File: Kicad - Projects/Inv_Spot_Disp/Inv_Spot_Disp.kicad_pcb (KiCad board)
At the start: 2 copper layers, 128.6 x 75.3 mm, 39 parts, among them J1 PWM_Out, J2 Power_Supply, J3 Trigger, J4 Prog, SW1 1, SW2 2, SW3 3, SW4 4, SW5 SW_Push, U1 STM32F030F4Px, U2 NHD-0420H1Z, U3 AMS1117-3.3, U4 LKS561, U5 L7805, U6 LTV-817S

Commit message: Cotações
Cotações
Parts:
- removed C12: 104, Capacitor_SMD:C_1206_3216Metric_Pad1.33x1.80mm_HandSolder
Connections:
- U1 pad 6: Current_Sense -> unconnected-(U1-PA0-Pad6)
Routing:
- net GND: track 346.7 -> 336.0 mm, vias 17 -> 16
- net Current_Sense: track 7.07 -> 0.00 mm
- net 5V: track 76.5 -> 78.0 mm, vias 2 -> 1
- net Net-(U2-VO): track 9.90 -> 8.50 mm
- net Enable: track 41.7 -> 40.5 mm
- net D7: track 22.9 -> 22.3 mm
- net RS: track 49.0 -> 48.5 mm
- net 3V3: vias 1 -> 0

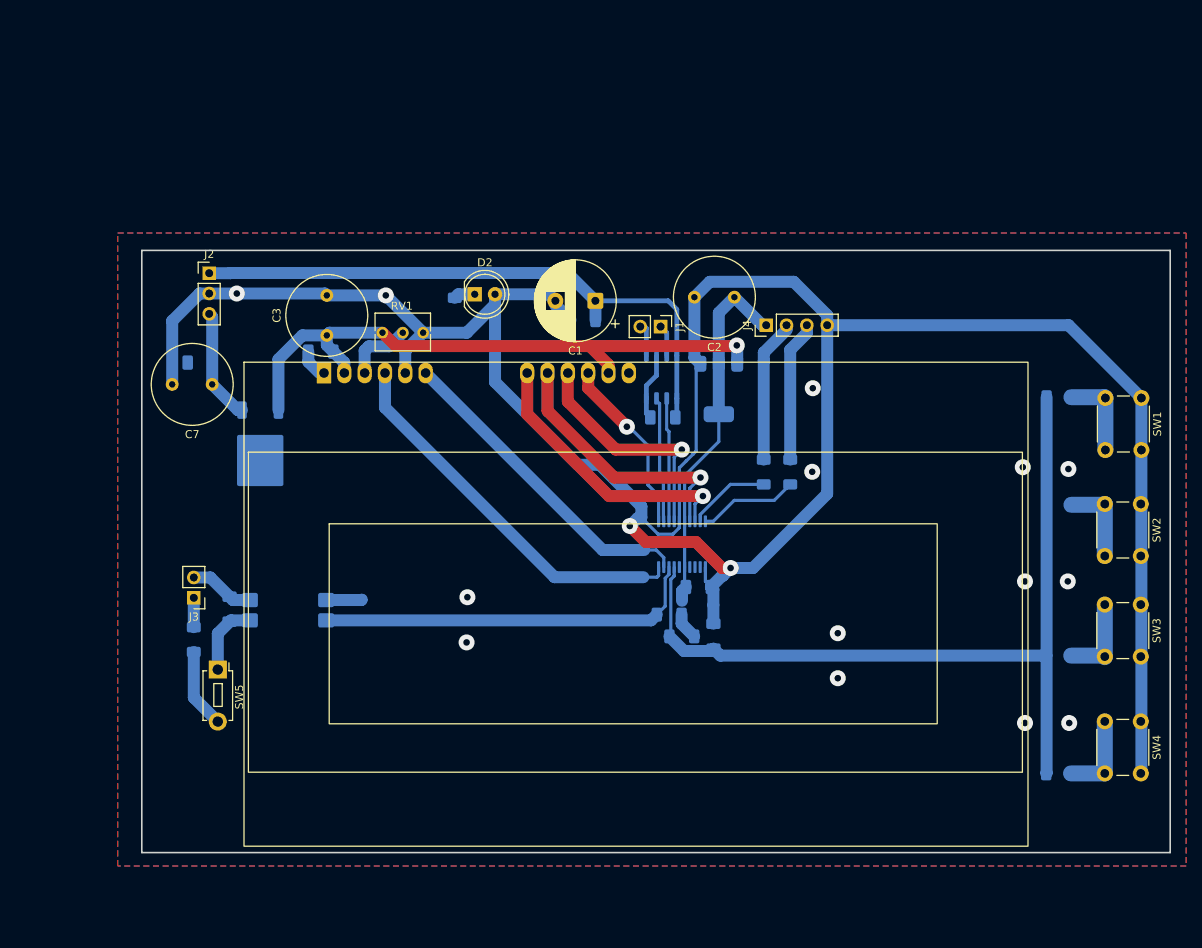
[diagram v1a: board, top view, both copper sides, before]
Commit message: Adicionada Fuaração
Adicionada furação de montagem na placa de display, 4 furos M3 nos cantos da placa
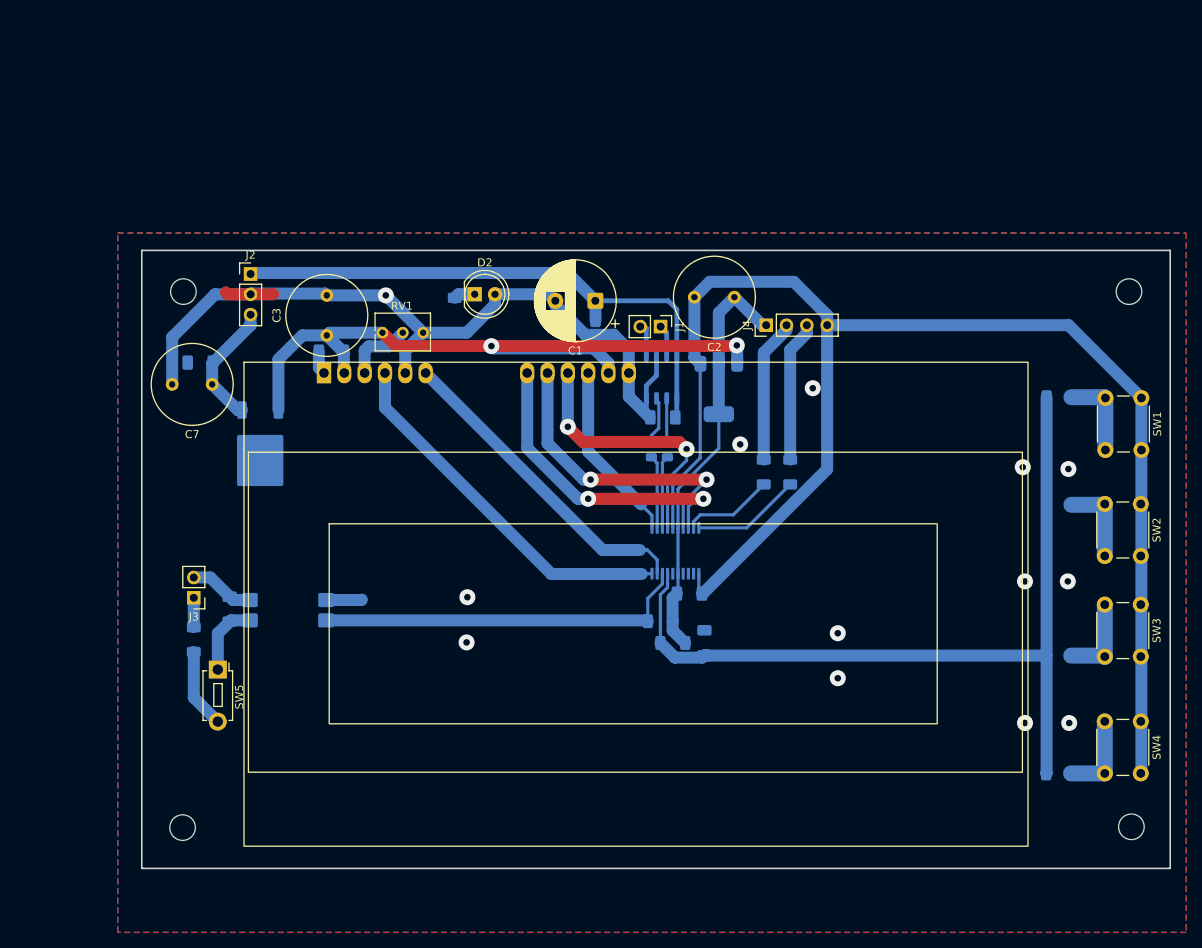
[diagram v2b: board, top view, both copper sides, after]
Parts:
- added R13: 470, Resistor_SMD:R_0805_2012Metric, B.Cu at (94.2, 74.3)
- added R15: 470, Resistor_SMD:R_0805_2012Metric, B.Cu at (92.2, 74.3)
- added REF**: MountingHole_3.2mm_M3, MountingHole:MountingHole_3.2mm_M3, F.Cu at (33.6, 121.5)
- added REF**: MountingHole_3.2mm_M3, MountingHole:MountingHole_3.2mm_M3, F.Cu at (33.7, 54.5)
- added REF**: MountingHole_3.2mm_M3, MountingHole:MountingHole_3.2mm_M3, F.Cu at (151.9, 54.5)
- added REF**: MountingHole_3.2mm_M3, MountingHole:MountingHole_3.2mm_M3, F.Cu at (152.2, 121.4)
- moved J2 5.18 mm to (42.1, 52.3)
- moved C4 1.40 mm to (97.0, 92.2)
- moved C6 1.40 mm to (98.8, 98.4)
- moved R1 1.40 mm to (94.9, 98.4)
- moved R9 1.40 mm to (93.3, 95.7)
- moved C5 1.33 mm to (52.2, 62.0)
- moved U1 1.17 mm to (95.2, 86.9)
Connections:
- U4 pad 2: PWM_H -> Net-(U4-Hin)
- U4 pad 3: PWM_L -> Net-(U4-Lin)
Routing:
- net GND: track 336.0 -> 294.3 mm, vias 16 -> 13
- net 5V: track 78.0 -> 90.5 mm, vias 1 -> 2
- net D7: track 22.3 -> 32.0 mm, vias 1 -> 0
- net PWM_L: track 15.7 -> 9.13 mm
- net PWM_H: track 15.5 -> 9.08 mm
- net Net-(U4-Lin): track 0.00 -> 6.04 mm
- net Net-(U4-Hin): track 0.00 -> 5.45 mm
- net 15V: track 76.3 -> 71.2 mm
- net D5: track 33.3 -> 37.8 mm, vias 1 -> 2
- net D4: track 34.9 -> 39.0 mm, vias 1 -> 2
- net D6: track 29.7 -> 33.6 mm, vias 1 -> 2
- net 3V3: track 49.6 -> 52.5 mm
- net RS: track 48.5 -> 46.3 mm
- net 7V: track 14.0 -> 15.8 mm
- net Trigger: track 48.2 -> 46.9 mm
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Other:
- board size 128.6 x 75.3 mm -> 128.6 x 77.2 mm

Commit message: Finalização da Nova Placa de Potência
Dissipadores reorientados e reposicionados para melhor fluxo de ar

Ajuste dos footprints para dissipadores

Adição de resistores na placa de display para melhor proteção do STM32 e redução do brilho da LCD
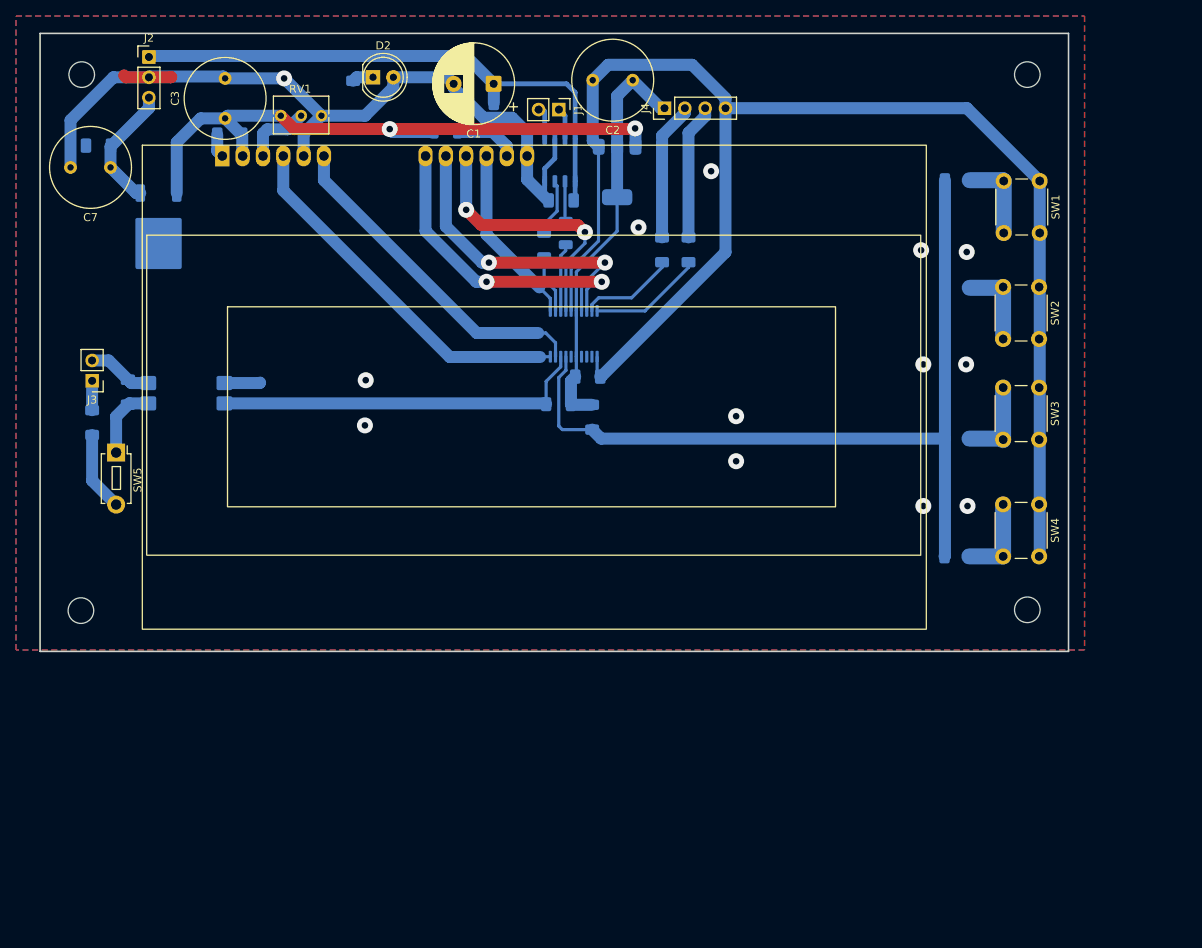
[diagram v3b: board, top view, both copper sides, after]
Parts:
- removed C6: 104, Capacitor_SMD:C_1206_3216Metric_Pad1.33x1.80mm_HandSolder
- added R16: 100, Resistor_SMD:R_1206_3216Metric, B.Cu at (66.5, 34.5)
- R1: value 2k -> 2k2
- R13, R15: value 470 -> 100; footprint Resistor_SMD:R_0805_2012Metric -> Resistor_SMD:R_1206_3216Metric
- R2: value 1k -> 10k
- R3: value 2k -> 4k7
- R4: value 4k -> 2k2
- R5: value 10k -> 1k
- R8: value 1k8 -> 2k2
- R9: value 3k3 -> 4k7
- moved R11 30.5 mm to (93.5, 49.3)
- moved R12 30.5 mm to (96.8, 49.3)
- moved REF** 30.1 mm to (139.2, 94.3)
- moved R1 30.0 mm to (84.8, 70.2), turned to -90 degrees
- moved R3 30.0 mm to (130.4, 54.0)
- moved U1 30.0 mm to (82.5, 59.8)
- moved C2 30.0 mm to (89.9, 28.1)
- moved J4 30.0 mm to (93.8, 31.6)
- moved C1 30.0 mm to (72.5, 28.5)
- moved C3 30.0 mm to (38.9, 32.9)
- moved C4 30.0 mm to (84.2, 65.1)
- moved C5 30.0 mm to (39.5, 34.9)
- moved C8 30.0 mm to (23.1, 36.2)
- moved C9 30.0 mm to (26.8, 67.1)
- moved D2 30.0 mm to (57.4, 27.7)
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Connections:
- U2 pad 15: 5V -> Net-(U2-A)
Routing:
- net 5V: track 90.5 -> 79.3 mm
- net Net-(U2-A): track 0.00 -> 7.75 mm
- net Enable: track 40.4 -> 42.1 mm
- net PWM_L: track 9.13 -> 7.43 mm
- net Net-(U4-Lin): track 6.04 -> 7.34 mm
- net 3V3: track 52.5 -> 51.8 mm
- net SWWDIO: track 11.5 -> 12.1 mm
- net SWCLK: track 13.7 -> 14.3 mm
- net Net-(J4-Pin_3): track 17.7 -> 17.0 mm
- net Net-(J4-Pin_2): track 18.0 -> 17.3 mm
- net PWM_H: track 9.08 -> 8.53 mm

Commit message: Preparação para Manufatura
Validação de footprints

Serigrafia movida para melhorar legibilidade

Backup de versão com trafo anterior salvo

Adição de snippet de código para ativação da proteção térmica
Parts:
- removed the REF** at (20.9, 94.4)
- removed the REF** at (21.0, 27.4)
- removed the REF** at (139.2, 27.4)
- removed the REF** at (139.2, 94.3)
- added R10: 4k7, Resistor_SMD:R_1206_3216Metric_Pad1.30x1.75mm_HandSolder, B.Cu at (88.5, 68.9)
- added R17: 2k2, Resistor_SMD:R_1206_3216Metric_Pad1.30x1.75mm_HandSolder, B.Cu at (106.2, 61.8)
- added REF**: Hexagonal-M3, Board_Fixation:Hexagonal-M3, B.Cu at (139.2, 20.5)
- added REF**: Hexagonal-M3, Board_Fixation:Hexagonal-M3, B.Cu at (20.9, 87.5)
- added REF**: Hexagonal-M3, Board_Fixation:Hexagonal-M3, B.Cu at (21.0, 20.6)
- added REF**: Hexagonal-M3, Board_Fixation:Hexagonal-M3, B.Cu at (139.2, 87.5)
- added U7: LTV-817S, Package_DIP:SMDIP-4_W9.53mm, B.Cu at (101.2, 67.9)
- moved C5 5.73 mm to (39.8, 40.6)
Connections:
- U1 pad 3: unconnected-(U1-PF1-Pad3) -> Temp_Sig
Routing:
- net 15V: track 71.2 -> 137.3 mm
- net GND: track 294.3 -> 231.1 mm, vias 13 -> 10
- net Temp_Sig: track 0.00 -> 18.2 mm
- net Net-(C11-Pad1): track 0.00 -> 3.38 mm
- net 5V: track 79.3 -> 82.3 mm
- net 3V3: track 51.8 -> 54.1 mm
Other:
- board text added: "Hexagonal-M3"
- board text added: "SPOTCAR INVERSORA PLACA DE DISPLAY REV 07/10/26 - V1.0.0"

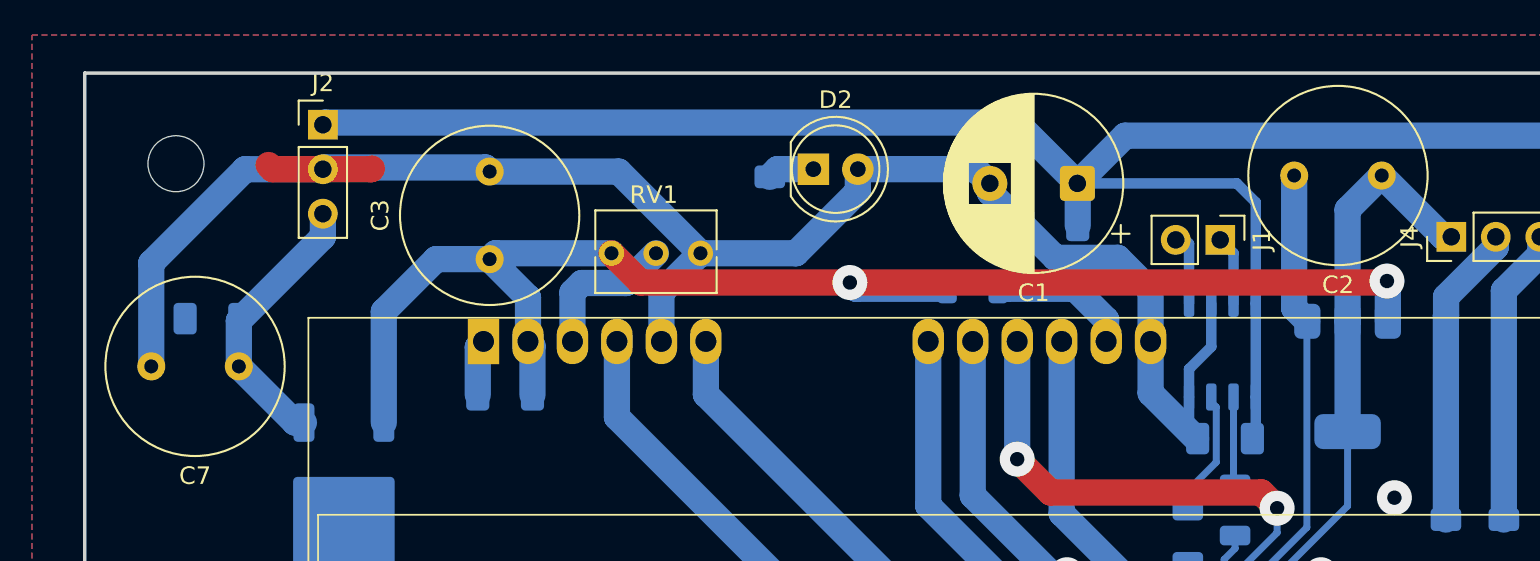
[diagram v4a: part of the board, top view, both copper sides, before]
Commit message: Finalização - Placa Protótipo
Versão final da placa protótipo - placa já validada

Alterações:
 - Melhoras no plano terra para retorno de potência
 - Blindagem das trilhas de PWM para os IGBTs inferiores
 - Alargamento das trilhas de saída para a retificação

Falta:
 - Colocar todos os SMDs no lado TOP da placa
 - Ajustar posição dos IGBTs e transformador
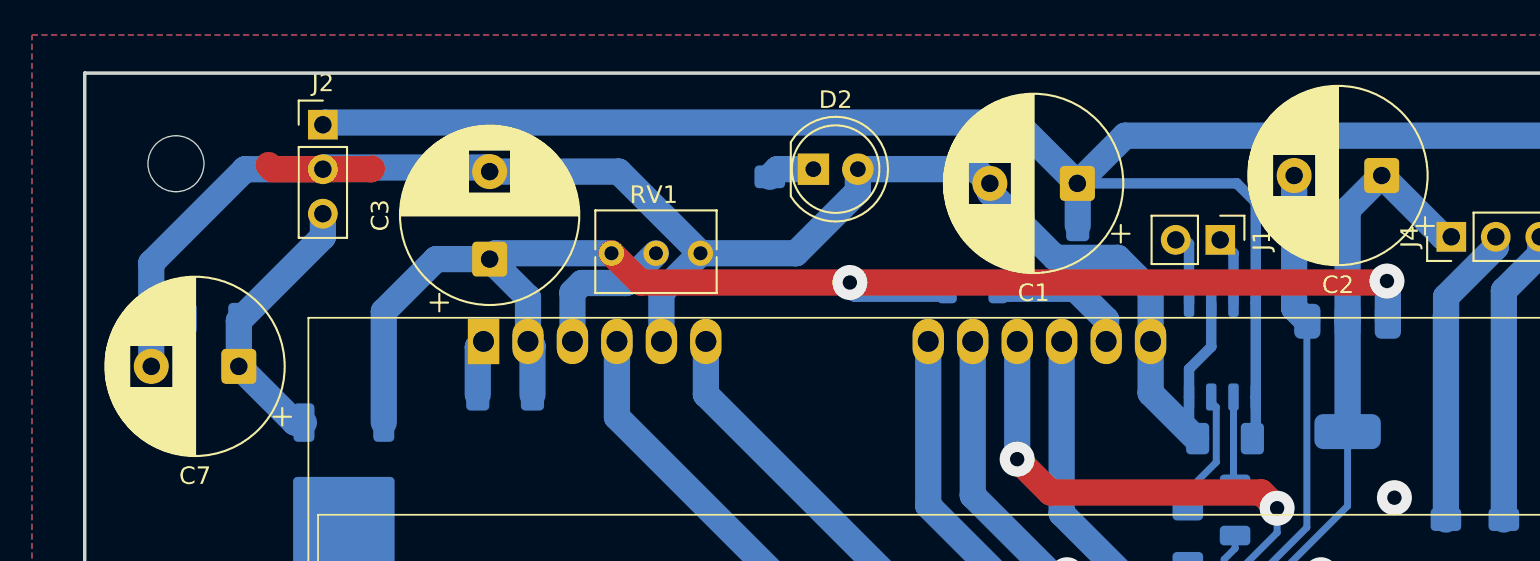
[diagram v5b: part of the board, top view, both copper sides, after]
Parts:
- C1: value 33u -> 100u
- C2, C3, C7: footprint Capacitor_THT:C_Radial_D10.0mm_H12.5mm_P5.00mm -> Capacitor_THT:CP_Radial_D10.0mm_P5.00mm
- R14: value 1k5 -> 2k2

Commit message: Ajustes para Produção
Ajustes de DFM para produção da placa

Falta ainda a nova versão com todos os SMDs e PTHs na mesma camada
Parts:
- moved C8 9.45 mm to (21.7, 45.6)
- moved C10 8.78 mm to (63.3, 26.6), turned to -90 degrees
- moved C5 2.40 mm to (39.8, 43.0)
- moved R14 2.32 mm to (52.6, 26.6)
- moved R16 2.10 mm to (65.6, 32.6)
- moved U5 1.41 mm to (30.3, 48.6)
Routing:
- net 7V: track 15.8 -> 22.4 mm
- net 5V: track 82.3 -> 86.0 mm
- net 15V: track 137.3 -> 134.9 mm
- net Net-(D2-K): track 2.67 -> 4.99 mm
- net GND: track 231.1 -> 233.2 mm
- net Net-(U2-A): track 7.75 -> 9.84 mm
